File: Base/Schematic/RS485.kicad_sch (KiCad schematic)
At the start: 8 parts, among them U3 CA-IS3052CW, U4 B0505S-1W

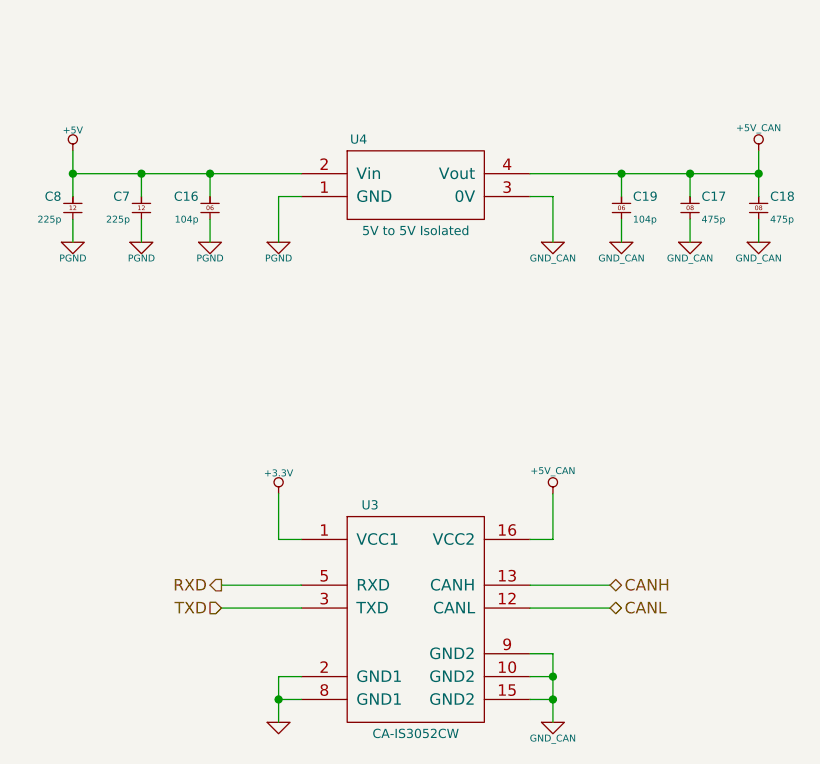
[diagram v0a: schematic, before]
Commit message: [Base 회로도 업데이트] - RS485 회로 추가
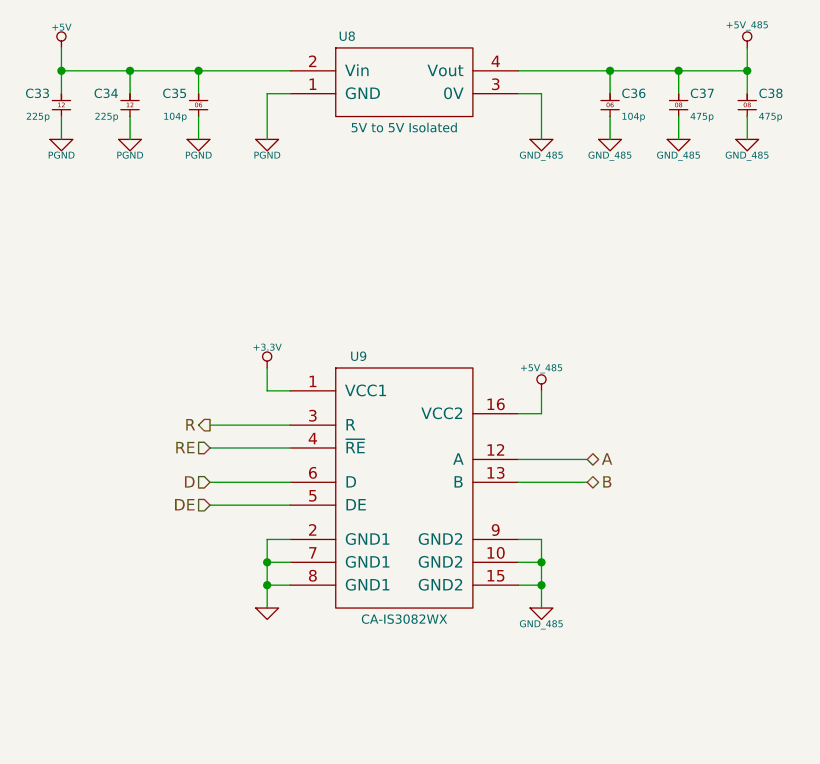
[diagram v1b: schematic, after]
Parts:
- removed C16, C19: 0603B104K500, SMC:0603, symbol Capacitor_MLCC:0603B104K500
- removed C17, C18: 0805B475K160, SMC:0805, symbol Capacitor_MLCC:0805B475K160
- removed C7, C8: 1206B225K500, SMC:0805, symbol Capacitor_MLCC:1206B225K500
- removed U3: CA-IS3052CW, SO:SOIC-16-WB, symbol Transceiver:CA-IS3052CW
- removed U4: B0505S-1W, ReSine PS:BXXS-1W, symbol Power_Module:B0505S-1W_ReSine PS
- added C33, C34: 1206B225K500, SMC:0805, symbol Capacitor_MLCC:1206B225K500
- added C35, C36: 0603B104K500, SMC:0603, symbol Capacitor_MLCC:0603B104K500
- added C37, C38: 0805B475K160, SMC:0805, symbol Capacitor_MLCC:0805B475K160
- added U8: B0505S-1W, ReSine PS:BXXS-1W, symbol Power_Module:B0505S-1W_ReSine PS
- added U9: CA-IS3082WX, SO:SOIC-16-WB, symbol Transceiver:CA-IS3082WX
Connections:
- net +3.3V: now also U9.1 (VCC1)
- net +5V: now also C33.2, C34.2, C35.2, U8.2 (Vin)
- net GND: now also U9.2 (GND1), U9.7 (GND1), U9.8 (GND1)
- net PGND: now also C33.1, C34.1, C35.1, U8.1 (GND)
- new net +5V_485: C36.2, C37.2, C38.2, U8.4 (Vout), U9.16 (VCC2)
- new net A: U9.12 (A)
- new net B: U9.13 (B)
- new net D: U9.6 (D)
- new net DE: U9.5 (DE)
- new net GND_485: C36.1, C37.1, C38.1, U8.3 (0V), U9.10 (GND2), U9.15 (GND2), U9.9 (GND2)
- new net R: U9.3 (R)
- new net RE: U9.4 (~{RE})

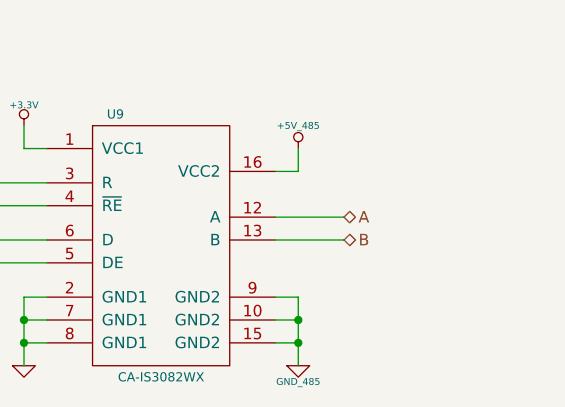
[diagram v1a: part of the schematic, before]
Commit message: [Base 회로도 업데이트] - RS485, CAN 보호회로 추가
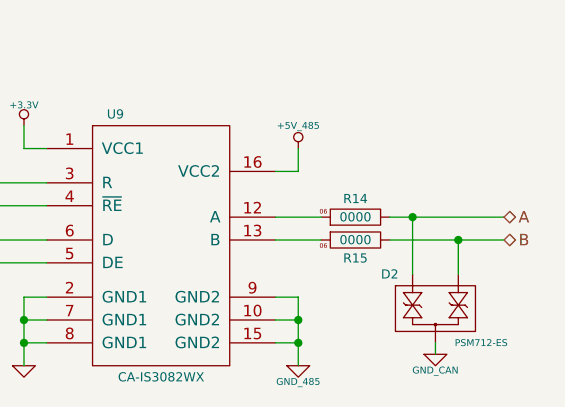
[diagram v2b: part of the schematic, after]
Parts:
- added D2: PSM712-ES, SOT:SOT23, symbol Diode_Protection:PSM712-ES
- added R14, R15: WR06X0000JTL, SMR:0603, symbol Resistor:WR06X0000JTL
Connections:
- net A: now also D2.1 (A2), R14.2; no longer U9.12 (A)
- net B: now also D2.2 (C1), R15.2; no longer U9.13 (B)
- new net: R14.1, U9.12 (A)
- new net: R15.1, U9.13 (B)
- new net GND_CAN: D2.3 (A1C2)

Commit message: [Base 회로도 업데이트] - AIN 입력 4개 추가
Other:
- company: (none) -> -
- title: (none) -> Open-PLC-Project
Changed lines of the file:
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@@
 	(generator_version "8.0")
 	(paper "A4")
+	(title_block
+		(title "Open-PLC-Project")
+		(date "2024-12-01")
+		(company "-")
+		(comment 1 "See the file \"LICENSE\" in the main directory of this archive for more details.")
+		(comment 2 "This file is subject to the terms and conditions of the MIT License.")
+		(comment 3 "Copyright (c) 2024 Yoon-Ki Hong")
+	)
 	(junction
 		(at 176.53 99.06)
@@
 		(dnp no)
 		(fields_autoplaced yes)
-		(property "Reference" "#PWR056"
+		(property "Reference" "#PWR065"
 			(at 118.11 63.5 0)
 			(effects
@@
 			(project "Open-PLC-Project"
 				(path "/0d177ca6-e392-45a0-9514-d370436392ef/d89ef6a0-3ba7-4277-9277-8f32ad685bed"
-					(reference "#PWR056")
+					(reference "#PWR065")
 					(unit 1)
 				)
@@
 		(dnp no)
 		(fields_autoplaced yes)
-		(property "Reference" "#PWR059"
+		(property "Reference" "#PWR068"
 			(at 133.35 86.614 0)
 			(effects
@@
 			(project "Open-PLC-Project"
 				(path "/0d177ca6-e392-45a0-9514-d370436392ef/d89ef6a0-3ba7-4277-9277-8f32ad685bed"
-					(reference "#PWR059")
+					(reference "#PWR068")
 					(unit 1)
 				)
@@
 		(dnp no)
 		(fields_autoplaced yes)
-		(property "Reference" "#PWR060"
+		(property "Reference" "#PWR069"
 			(at 133.35 115.57 0)
 			(effects
@@
 			(project ""
 				(path "/0d177ca6-e392-45a0-9514-d370436392ef/d89ef6a0-3ba7-4277-9277-8f32ad685bed"
-					(reference "#PWR060")
+					(reference "#PWR069")
 					(unit 1)
 				)
@@
 		(dnp no)
 		(fields_autoplaced yes)
-		(property "Reference" "#PWR055"
+		(property "Reference" "#PWR064"
 			(at 110.49 63.5 0)
 			(effects
@@
 			(project "Open-PLC-Project"
 				(path "/0d177ca6-e392-45a0-9514-d370436392ef/d89ef6a0-3ba7-4277-9277-8f32ad685bed"
-					(reference "#PWR055")
+					(reference "#PWR064")
 					(unit 1)
 				)
@@
 		(dnp no)
 		(fields_autoplaced yes)
-		(property "Reference" "#PWR058"
+		(property "Reference" "#PWR067"
 			(at 133.35 63.5 0)
 			(effects
@@
 			(project "Open-PLC-Project"
 				(path "/0d177ca6-e392-45a0-9514-d370436392ef/d89ef6a0-3ba7-4277-9277-8f32ad685bed"
-					(reference "#PWR058")
+					(reference "#PWR067")
 					(unit 1)
 				)
@@
 		(dnp no)
 		(fields_autoplaced yes)
-		(property "Reference" "#PWR054"
+		(property "Reference" "#PWR063"
 			(at 110.49 51.054 0)
 			(effects
@@
 			(project "Open-PLC-Project"
 				(path "/0d177ca6-e392-45a0-9514-d370436392ef/d89ef6a0-3ba7-4277-9277-8f32ad685bed"
-					(reference "#PWR054")
+					(reference "#PWR063")
 					(unit 1)
 				)
@@
 		(dnp no)
 		(fields_autoplaced yes)
-		(property "Reference" "#PWR057"
+		(property "Reference" "#PWR066"
 			(at 125.73 63.5 0)
 			(effects
@@
 			(project "Open-PLC-Project"
 				(path "/0d177ca6-e392-45a0-9514-d370436392ef/d89ef6a0-3ba7-4277-9277-8f32ad685bed"
-					(reference "#PWR057")
+					(reference "#PWR066")
 					(unit 1)
 				)
